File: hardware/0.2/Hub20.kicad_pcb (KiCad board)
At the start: 2 copper layers, 89 x 124 mm, 164 parts, among them J1 USB_C_Receptacle_USB2.0, J2 USB_C_Receptacle_USB2.0, J3 USB_C_Receptacle_USB2.0, J4 USB_C_Receptacle_USB2.0, Q1 DTC123J, Q2 BSS138, SW1 SW_Push, SW10 MX_RGB, SW11 MX_RGB, SW12 MX_RGB, SW13 Rotary_Encoder_Switch, SW14 MX_RGB, SW15 MX_RGB, SW16 MX_RGB, SW17 MX_RGB, SW18 MX_RGB, SW19 MX_RGB, SW2 MX_RGB, SW20 MX_RGB, SW21 MX_RGB, SW22 MX_RGB, SW23 MX_RGB, SW3 MX_RGB, SW4 MX_RGB, SW5 MX_RGB, SW6 MX_RGB, SW7 Rotary_Encoder_Switch, SW8 MX_RGB, SW9 MX_RGB, U1 AP2112K-3.3, U2 USBLC6-2SC6, U3 STM32F072C8Tx, U5 CY7C65632-28LTXCT, U6 USBLC6-2SC6, U7 USBLC6-2SC6, U8 USBLC6-2SC6, Y1 12MHz

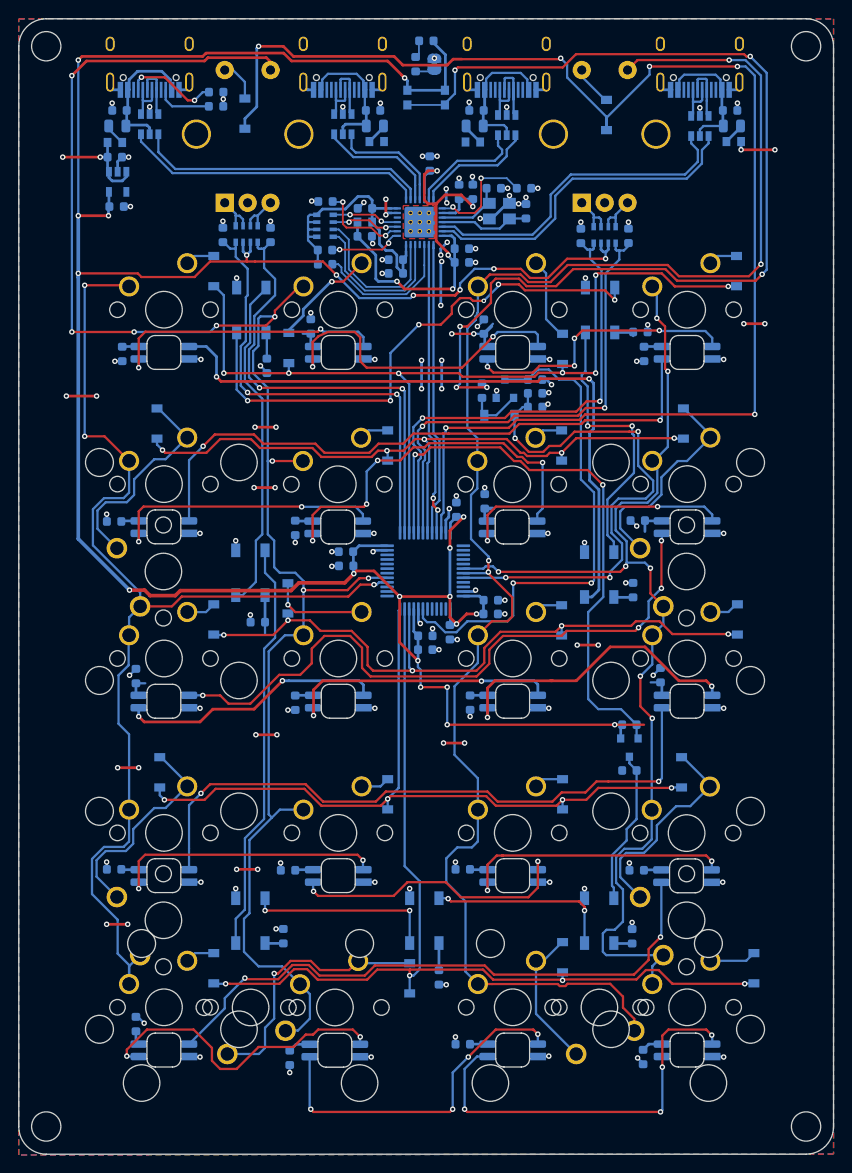
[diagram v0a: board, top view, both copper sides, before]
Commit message: side mounted rst + slik cleanup
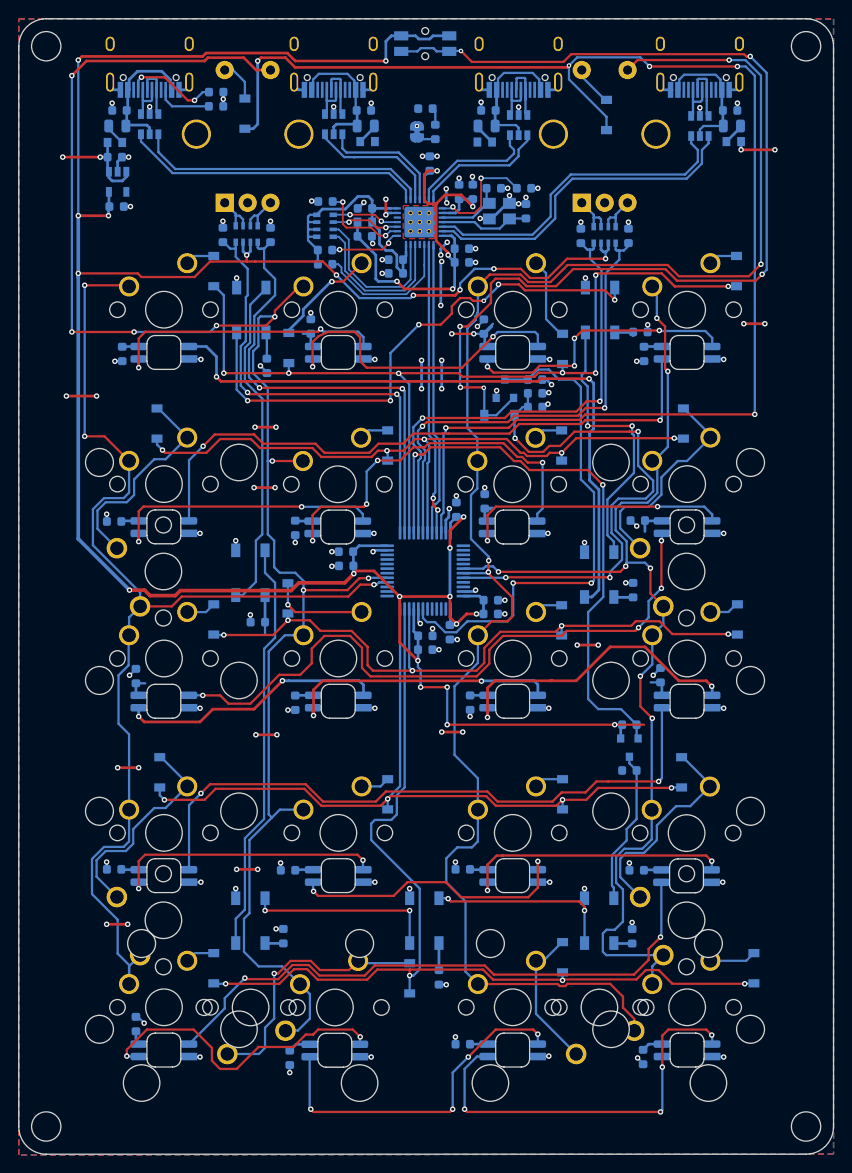
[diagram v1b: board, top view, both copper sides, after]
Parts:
- removed R1: 2K2, Resistor_SMD:R_0603_1608Metric
- LOGO3: footprint josh-logos:josh-johnson-logo-8_6x1_5 -> josh-logos:josh-johnson-logo-11x2
- LOGO5: footprint josh-logos:OSHW_Logo_3.6x3.6_F.Mask -> josh-logos:OSHW-Logo2_9.8x8mm_Mask
- R14: value 2K2 -> 5K1
- SW1: value SW_Push -> SIDE; footprint josh-buttons-switches:SW_Push_KMR2 -> josh-buttons-switches:Panasonic_EVQPUL_EVQPUC
- SW13, SW7: value Rotary_Encoder_Switch -> EC11
- moved LOGO1 50.3 mm to (177.6, 89.3), turned to 270 degrees
- moved LOGO3 46.6 mm to (175.0, 90.1), turned to 270 degrees
- moved LOGO5 22.4 mm to (141.1, 121.8)
- moved LOGO2 12.2 mm to (140.2, 111.4)
- moved R14 7.71 mm to (142.2, 45.0)
- moved JP1 7.64 mm to (140.2, 45.0)
- moved D32 7.40 mm to (141.1, 42.4), turned to 180 degrees
- moved SW1 5.90 mm to (141.1, 35.3)
- moved C59 1.30 mm to (148.0, 42.6)
- moved F3 1.30 mm to (147.8, 44.3)
- moved J3 1.30 mm to (151.3, 37.2)
- moved U7 1.30 mm to (151.3, 44.2)
- moved FB4 1.30 mm to (147.6, 46.0)
- moved C58 1.00 mm to (134.4, 42.6)
- moved F2 1.00 mm to (134.6, 44.3)
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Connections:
- D32 pad 2: +3V3 -> +5V
- SW1 pad 2: Net-(R1-Pad2) -> Net-(D1-Pad2)
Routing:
- net Net-(R1-Pad2): track 115.4 -> 0.00 mm, vias 6 -> 0
- net Net-(D1-Pad2): track 5.99 -> 118.7 mm, vias 0 -> 6
- net +3V3: track 301.9 -> 297.1 mm
- net /R5: track 107.1 -> 111.2 mm
- net /USB Hub/D2_D-: track 13.2 -> 14.5 mm
- net /USB Hub/D2_D+: track 13.2 -> 14.5 mm
- net /USB Hub/D1_D-: track 13.6 -> 14.7 mm
- net /R0: track 157.5 -> 156.5 mm
- net /USB Hub/D1_D+: track 13.0 -> 14.0 mm
- net /C1: track 190.8 -> 189.9 mm

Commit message: stop touching the design josh
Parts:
- moved C44 0.11 mm to (148.7, 51.1)
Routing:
- net +5V: track 111.4 -> 121.3 mm, vias 28 -> 40
- net GND: track 135.2 -> 131.8 mm, vias 113 -> 109
- net +3.3VA: track 50.6 -> 48.5 mm
- net Net-(R10-Pad1): track 12.3 -> 11.0 mm
- net /USB_D+: track 32.3 -> 33.4 mm
- net /USB Hub/D1_D+: track 14.0 -> 14.9 mm
- net /USB Hub/D3_D-: track 36.1 -> 36.9 mm
- net /C1: track 189.9 -> 189.3 mm
- net /USB Hub/D2_D-: track 14.5 -> 15.0 mm

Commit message: update BOM
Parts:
- added D31: SK6812 PNP, josh-keyboard:DUMMY_SK6812MINI-E, B.Cu at (150.7, 145.2)
- added D33: SK6812 PNP, josh-keyboard:DUMMY_SK6812MINI-E, B.Cu at (131.3, 145.2)
- added D34: SK6812 PNP, josh-keyboard:DUMMY_SK6812MINI-E, B.Cu at (112.6, 145.2)
- added D35: SK6812 PNP, josh-keyboard:DUMMY_SK6812MINI-E, B.Cu at (150.7, 126.2)
- added D36: SK6812 PNP, josh-keyboard:DUMMY_SK6812MINI-E, B.Cu at (112.6, 126.2)
- added D37: SK6812 PNP, josh-keyboard:DUMMY_SK6812MINI-E, B.Cu at (150.7, 69.0)
- added D38: SK6812 PNP, josh-keyboard:DUMMY_SK6812MINI-E, B.Cu at (169.8, 145.2)
- added D39: SK6812 PNP, josh-keyboard:DUMMY_SK6812MINI-E, B.Cu at (131.7, 126.2)
- added D40: SK6812 PNP, josh-keyboard:DUMMY_SK6812MINI-E, B.Cu at (112.6, 88.1)
- added D41: SK6812 PNP, josh-keyboard:DUMMY_SK6812MINI-E, B.Cu at (131.7, 69.0)
- added D42: SK6812 PNP, josh-keyboard:DUMMY_SK6812MINI-E, B.Cu at (169.7, 126.2)
- added D43: SK6812 PNP, josh-keyboard:DUMMY_SK6812MINI-E, B.Cu at (169.8, 88.1)
- added D44: SK6812 PNP, josh-keyboard:DUMMY_SK6812MINI-E, B.Cu at (169.8, 69.0)
- added D45: SK6812 PNP, josh-keyboard:DUMMY_SK6812MINI-E, B.Cu at (112.6, 69.0)
- added D46: SK6812 PNP, josh-keyboard:DUMMY_SK6812MINI-E, B.Cu at (169.8, 107.2)
- added D47: SK6812 PNP, josh-keyboard:DUMMY_SK6812MINI-E, B.Cu at (150.7, 88.1)
- added D48: SK6812 PNP, josh-keyboard:DUMMY_SK6812MINI-E, B.Cu at (112.6, 107.2)
- added D49: SK6812 PNP, josh-keyboard:DUMMY_SK6812MINI-E, B.Cu at (150.7, 107.2)
- added D50: SK6812 PNP, josh-keyboard:DUMMY_SK6812MINI-E, B.Cu at (131.6, 88.1)
- added D51: SK6812 PNP, josh-keyboard:DUMMY_SK6812MINI-E, B.Cu at (131.7, 107.2)
- C44, C45: value 22p -> 15p
- SW1: value SIDE -> EVQPUL
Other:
- net class Default: via_dia 0.5 -> 0.6; via_drill 0.25 -> 0.3
- rule via_min_drill: 0.25 -> 0.3
- rule via_min_size: 0.5 -> 0.6

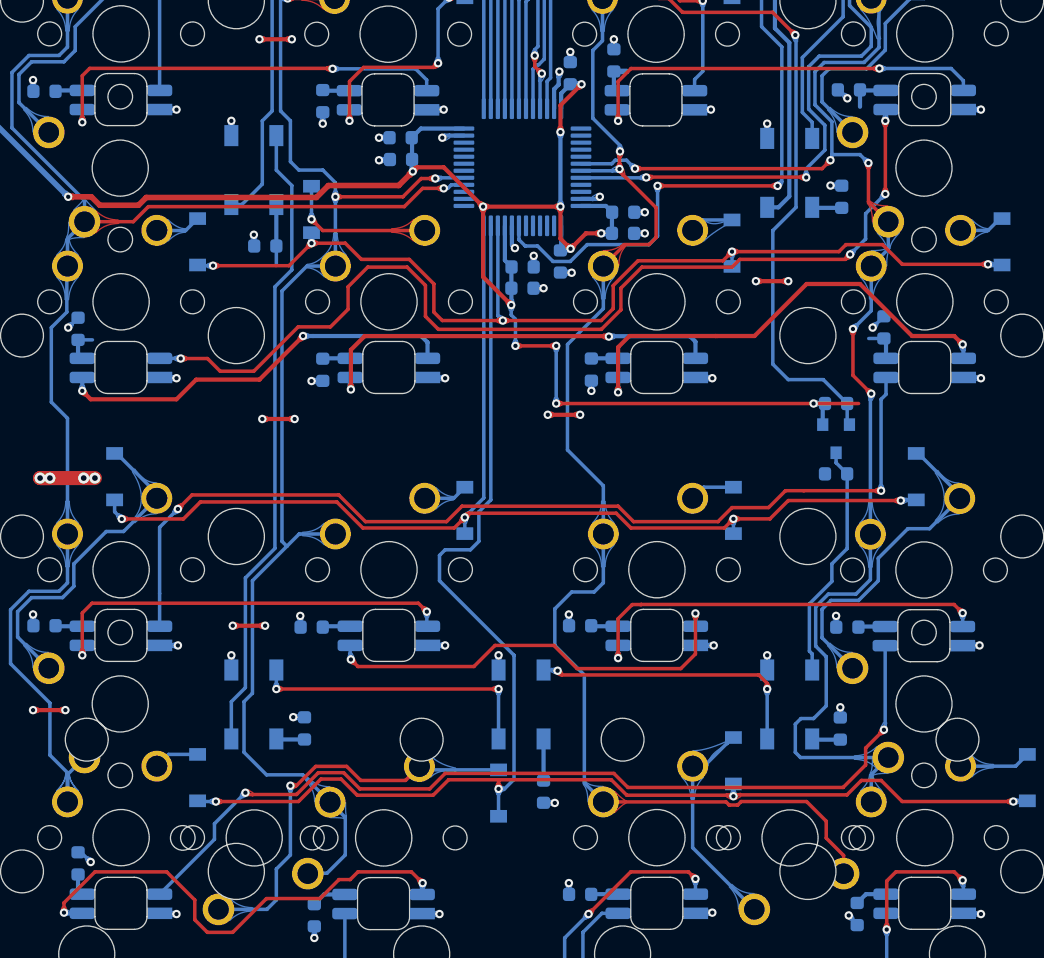
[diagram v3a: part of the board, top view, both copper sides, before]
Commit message: limit 2U to 3 pin only
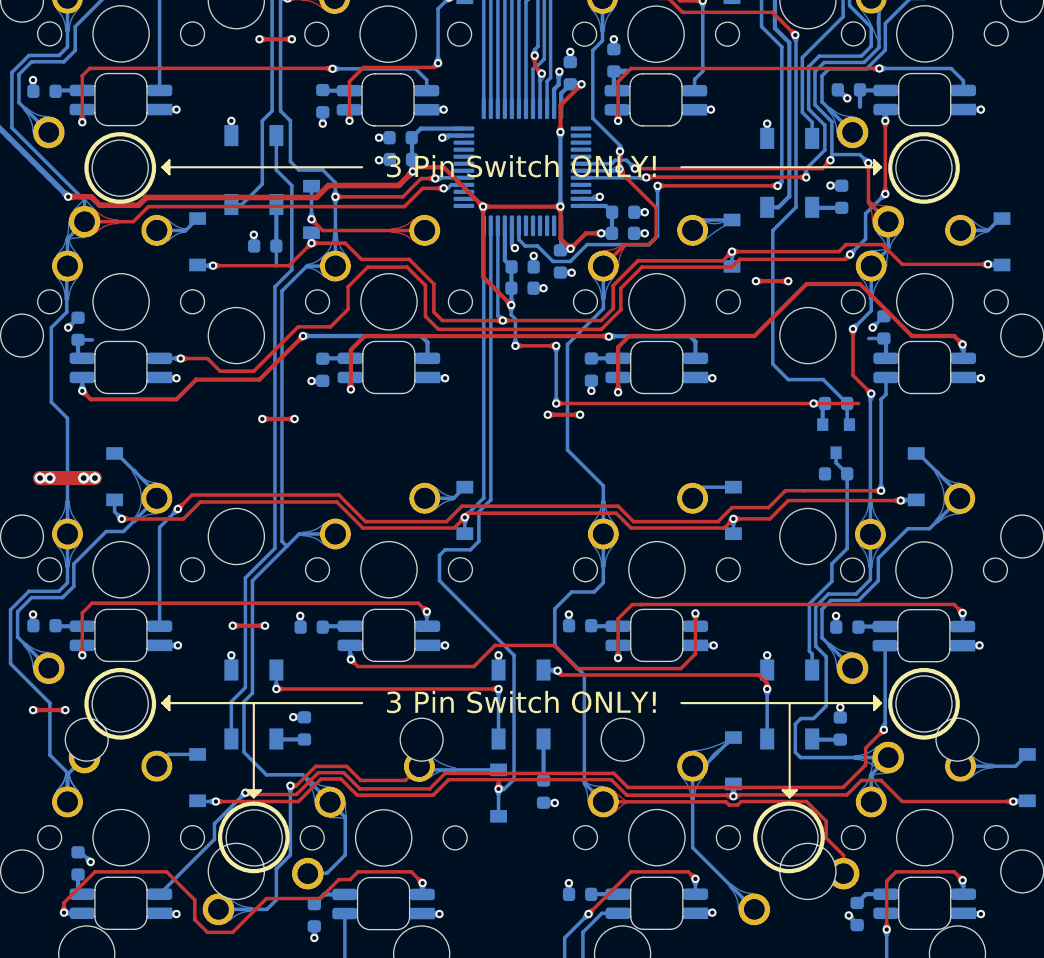
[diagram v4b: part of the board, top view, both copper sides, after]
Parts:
- D31, D33, D34, D35, D36, D37, D38, D39, D40, D41, D42, D43, D44, D45, D46, D47, D48, D49, D50, D51: value SK6812 PNP -> SK6812MINI-E
- MX1, MX2: footprint josh-keyboard:MXOnly-2U-NoLED -> josh-keyboard:MXOnly-2U-NoLED-3PIN
- MX3, MX4, MX5, MX6: footprint josh-keyboard:MXOnly-2U-ReversedStabilizers-NoLED -> josh-keyboard:MXOnly-2U-ReversedStabilizers-NoLED-3PIN
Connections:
- J1 pad A8: (no net) -> Net-(J1-PadA8)
- J1 pad B8: (no net) -> Net-(J1-PadB8)
- J2 pad A5: (no net) -> Net-(J2-PadA5)
- J2 pad A8: (no net) -> Net-(J2-PadA8)
- J2 pad B5: (no net) -> Net-(J2-PadB5)
- J2 pad B8: (no net) -> Net-(J2-PadB8)
- J3 pad A5: (no net) -> Net-(J3-PadA5)
- J3 pad A8: (no net) -> Net-(J3-PadA8)
- J3 pad B5: (no net) -> Net-(J3-PadB5)
- J3 pad B8: (no net) -> Net-(J3-PadB8)
- J4 pad A5: (no net) -> Net-(J4-PadA5)
- J4 pad A8: (no net) -> Net-(J4-PadA8)
- J4 pad B5: (no net) -> Net-(J4-PadB5)
- J4 pad B8: (no net) -> Net-(J4-PadB8)
- SW23 pad 4: (no net) -> Net-(SW23-Pad4)
- U1 pad 4: (no net) -> Net-(U1-Pad4)
- U3 pad 13: (no net) -> Net-(U3-Pad13)
- U3 pad 14: (no net) -> Net-(U3-Pad14)
- U3 pad 15: (no net) -> Net-(U3-Pad15)
- U3 pad 18: (no net) -> Net-(U3-Pad18)
- U3 pad 19: (no net) -> Net-(U3-Pad19)
- U3 pad 2: (no net) -> Net-(U3-Pad2)
- U3 pad 20: (no net) -> Net-(U3-Pad20)
- U3 pad 21: (no net) -> Net-(U3-Pad21)
- U3 pad 22: (no net) -> Net-(U3-Pad22)
- U3 pad 3: (no net) -> Net-(U3-Pad3)
- U3 pad 37: (no net) -> Net-(U3-Pad37)
- U3 pad 38: (no net) -> Net-(U3-Pad38)
- U3 pad 39: (no net) -> Net-(U3-Pad39)
- U3 pad 4: (no net) -> Net-(U3-Pad4)
- U3 pad 40: (no net) -> Net-(U3-Pad40)
- U3 pad 41: (no net) -> Net-(U3-Pad41)
- U3 pad 45: (no net) -> Net-(U3-Pad45)
- U3 pad 46: (no net) -> Net-(U3-Pad46)
- U3 pad 5: (no net) -> Net-(U3-Pad5)
- U3 pad 6: (no net) -> Net-(U3-Pad6)
- U5 pad 18: (no net) -> Net-(U5-Pad18)
- U5 pad 26: (no net) -> Net-(U5-Pad26)
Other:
- board text added: "3 Pin Switch ONLY!"
